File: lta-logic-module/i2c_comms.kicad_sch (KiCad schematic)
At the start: 9 parts

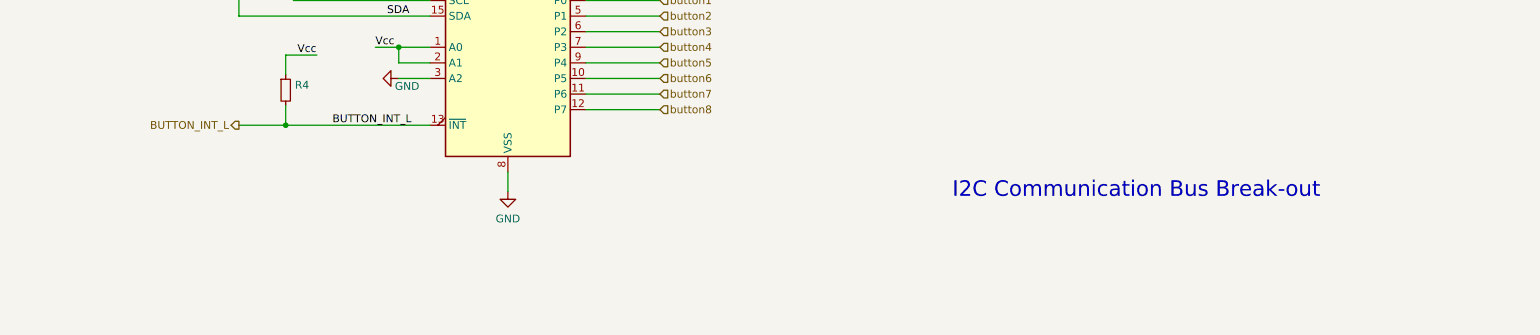
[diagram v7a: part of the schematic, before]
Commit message: Generate logic module 2022-05-08 v1.0 fab documentation.
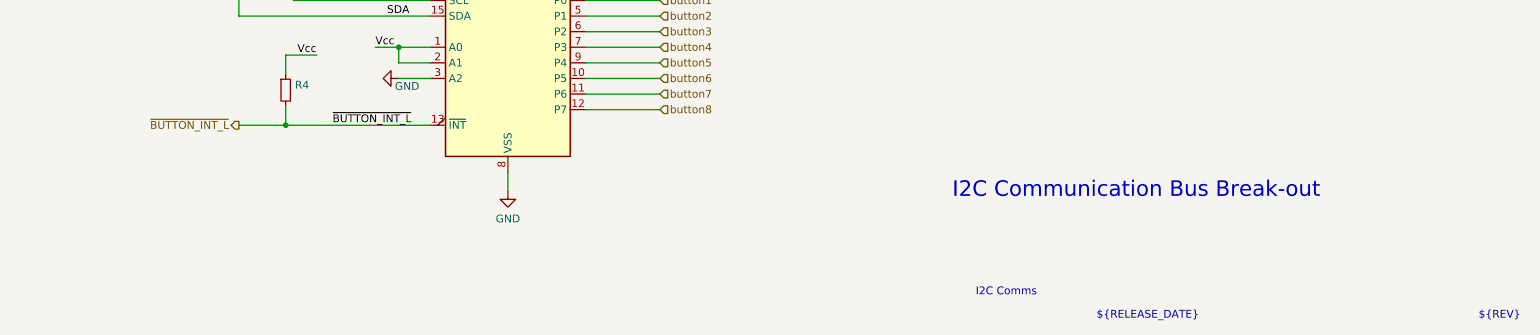
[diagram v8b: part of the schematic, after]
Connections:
- net BUTTON_INT_L renamed ~{BUTTON_INT_L}
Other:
- note added: "${RELEASE_DATE}"
- note added: "${REV}"
- note added: "I2C Comms"
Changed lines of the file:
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@@
+    (effects (font (size 1.27 1.27)) (justify left bottom))
+  )
+  (text "${RELEASE_DATE}" (at 206.375 194.31 0)
     (effects (font (size 1.27 1.27)) (justify left bottom))
   )
   (text "MOSFET bank 0\n" (at 120.015 31.75 0)
+    (effects (font (size 1.27 1.27)) (justify left bottom))
+  )
+  (text "${REV}" (at 268.605 194.31 0)
     (effects (font (size 1.27 1.27)) (justify left bottom))
   )
@@
   )
   (text "3V3 logic through I2C bus" (at 32.385 17.145 0)
+    (effects (font (size 1.27 1.27)) (justify left bottom))
+  )
+  (text "I2C Comms" (at 186.69 190.5 0)
     (effects (font (size 1.27 1.27)) (justify left bottom))
   )
@@
     (effects (font (size 1.27 1.27)) (justify left bottom))
   )
-  (label "BUTTON_INT_L" (at 81.915 162.56 0)
+  (label "~{BUTTON_INT_L}" (at 81.915 162.56 0)
     (effects (font (size 1.27 1.27)) (justify left bottom))
   )
@@
     (effects (font (size 1.27 1.27)) (justify left))
   )
-  (hierarchical_label "BUTTON_INT_L" (shape output) (at 66.675 162.56 180)
+  (hierarchical_label "~{BUTTON_INT_L}" (shape output) (at 66.675 162.56 180)
     (effects (font (size 1.27 1.27)) (justify right))
   )
